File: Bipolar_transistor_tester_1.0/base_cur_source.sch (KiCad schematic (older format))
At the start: 38 parts

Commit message: tester up
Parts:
- removed D? (x2): 1N4740A, Diode_THT:D_DO-41_SOD81_P10.16mm_Horizontal, symbol Diode:1N47xxA
- removed Q?: AO3400A, Package_TO_SOT_SMD:SOT-23, symbol Transistor_FET:AO3400A
- removed Q?: AO3401A, Package_TO_SOT_SMD:SOT-23, symbol Transistor_FET:AO3401A
- removed R? (x2): 270, Resistor_SMD:R_0805_2012Metric, symbol Device:R
- added C26, C27, C28, C29: 100n, Capacitor_SMD:C_0805_2012Metric, symbol Device:C
- added D12, D13: 1N4744A, Diode_THT:D_DO-41_SOD81_P10.16mm_Horizontal, symbol Diode:1N47xxA
- added Q7: IRFR9024 [DPAK], Package_TO_SOT_SMD:TO-252-2, symbol Transistor_FET:IRF4905
- added Q8: IRF640 [DPAK], Package_TO_SOT_SMD:TO-252-2, symbol Transistor_FET:IRF540N
- added R48, R60, R61, R66, R67, R70, R71, R72: 1k 1%, Resistor_SMD:R_0805_2012Metric, symbol Device:R
- added R62, R63: 2.2k, Resistor_SMD:R_0805_2012Metric, symbol Device:R
- added U36: PVN012, Package_DIP:DIP-6_W7.62mm, symbol Relay_SolidState:PVN012
- added U43: PVG612, Package_DIP:DIP-6_W7.62mm, symbol Relay_SolidState:PVG612
- R56, R57: renamed from R?; value 50k -> 51k
- R58, R59: renamed from R?; value 100 1% -> 10 1%
- R64, R65: renamed from R?; value 50k 1% -> 200k 1%
- R68, R69: renamed from R?; value 10M 1% -> 20M 1%
- gave numbers to parts that had none: 22
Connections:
- net +15V: now also C27.1
- net +24V: now also C28.1
- net -15V: now also C26.1
- net -24V: now also C29.1
- net GND: now also C26.2, C27.2, C28.2, C29.2
- net out: now also U43.6
- net at IC5.2, R59.2, R65.2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: now also D13.2 (A), Q8.3 (S)
- net at IC5.6: now also R63.2
- net at IC4.2, R58.2, R64.2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: now also D12.1 (K), Q7.3 (S)
- net at IC4.6: now also R62.2
- net at U37.1: now also R60.2
- net 2_bcs2: now reaches U37.2
- net 2_bcs2: now also U38.2
- net at U39.1: now also R66.2
- net 2_bcs3: now reaches U39.2
- net 2_bcs3: now also U40.2
- net at U41.1: now also R70.2
- net 2_bcs4: now reaches U41.2
- net 2_bcs4: now also U42.2
- net at U38.1: now also R61.2
- net at U40.1: now also R67.2
- net at U42.1: now also R71.2
- net dac_in: no longer names the net of R49.1, U35.3 (+), U35.5 (+)
- net dac_in: now also U36.6
- new net: D13.1 (K), Q8.1 (G), R63.1
- new net: D12.2 (A), Q7.1 (G), R62.1
- new net: Q7.2 (D), Q8.2 (D), U43.4
- new net: R48.2, U36.1
- new net: R72.2, U43.1
- new net 2_bcs1: U36.2
- new net 2_bcs5: U43.2
- new net 2_com_an: R48.1, R60.1, R61.1, R66.1, R67.1, R70.1, R71.1, R72.1
- new net dac1: U36.4
- no-connect marks 6 -> 12
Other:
- moved on the sheet: R58, R64, R65, R68, R69

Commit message: tester up
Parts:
- removed R59: 10 1%, Resistor_SMD:R_0805_2012Metric, symbol Device:R
- added R79: 10 1% 0.5W, Resistor_THT:R_Axial_DIN0309_L9.0mm_D3.2mm_P12.70mm_Horizontal, symbol Device:R
- Q7: value IRFR9024 [DPAK] -> IRFR9024
- Q8: value IRF640 [DPAK] -> IRF640
- R78: renamed from R58; value 10 1% -> 10 1% 0.5W; footprint Resistor_SMD:R_0805_2012Metric -> Resistor_THT:R_Axial_DIN0309_L9.0mm_D3.2mm_P12.70mm_Horizontal
- R84: renamed from R64; value 200k 1% -> 20k 1%
- R85: renamed from R65; value 200k 1% -> 20k 1%
- renumbered R48 to R68, R49 to R69, R50 to R70, R51 to R71, R52 to R72, R53 to R73, R54 to R74, R55 to R75, R56 to R76, R57 to R77, R60 to R80, R61 to R81, R62 to R82, R63 to R83, R66 to R86, R67 to R87, R68 to R88, R69 to R89, R70 to R90, R71 to R91, R72 to R92
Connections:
- net +15V: no longer R72.1
- net +24V: now also R72.1
- net -15V: no longer R75.2
- net -24V: now also R75.2
- net at D13.2 (A), IC5.2, Q8.3 (S)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: now also R79.2
- net at U38.6: now also R79.1

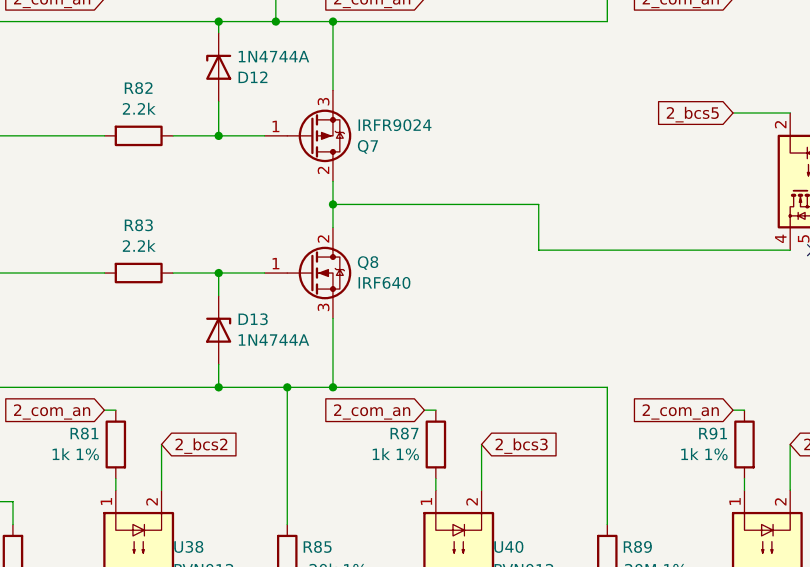
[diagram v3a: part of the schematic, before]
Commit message: edit resistors cpc1977
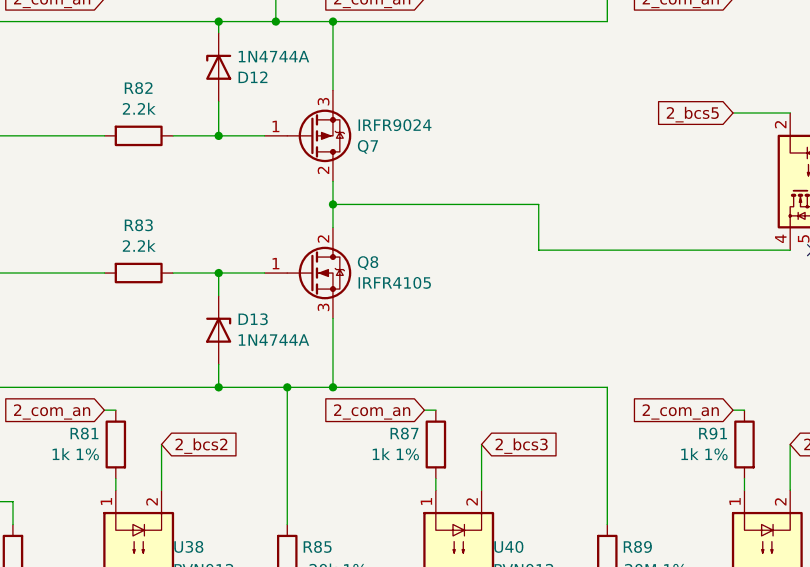
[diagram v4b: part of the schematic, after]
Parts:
- Q8: value IRF640 -> IRFR4105
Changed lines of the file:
@@
 AR Path="/625CBCFC/6269E0DD" Ref="Q8"  Part="1"
 F 0 "Q8" H 8155 4096 50  0000 L CNN
-F 1 "IRF640" H 8155 4005 50  0000 L CNN
+F 1 "IRFR4105" H 8155 4005 50  0000 L CNN
 F 2 "Package_TO_SOT_SMD:TO-252-2" H 8200 3975 50  0001 L CIN
 F 3 "" H 7950 4050 50  0001 L CNN
